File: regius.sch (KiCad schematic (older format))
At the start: 39 parts, among them J1 Conn_01x02, J10 Conn_01x02, J16 Conn_01x04, J7 Conn_01x02, J9 Conn_01x02, SW1 Reset, U5 LM1117-3.3

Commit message: update schematic
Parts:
- removed C? (x8): C_Small, symbol Device:C_Small
- removed D? (x5): D_TVS, symbol Device:D_TVS
- removed J10, J9: Conn_01x02, Connector_PinHeader_2.54mm:PinHeader_1x02_P2.54mm_Vertical, symbol Connector_Generic:Conn_01x02
- removed J16: Conn_01x04, Connector_PinHeader_2.54mm:PinHeader_1x04_P2.54mm_Vertical, symbol Connector_Generic:Conn_01x04
- removed R?: R_Small, symbol Device:R_Small
- added C? (x12): C_Small, symbol Device:C_Small
- added FB?: Ferrite_Bead_Small, symbol Device:Ferrite_Bead_Small
- added R?: R330, Resistor_SMD:R_0603_1608Metric, symbol Device:R
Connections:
- wire segments 150 -> 115
- no-connect marks 0 -> 5
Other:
- moved on the sheet: C10, C8, C9, C?, J1, J7, J?, R1, R2, R3, R6, SW1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

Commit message: debug port
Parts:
- added J?: Conn_02x05_Counter_Clockwise, symbol Connector_Generic:Conn_02x05_Counter_Clockwise
- added R?: R1K, Resistor_SMD:R_0603_1608Metric, symbol Device:R
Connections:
- wire segments 115 -> 132
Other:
- moved on the sheet: R1, R2, R3
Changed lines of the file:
@@
 Text Label 22400 6600 0    50   ~ 0
 txd0
-Text Label 12400 6000 0    50   ~ 0
+Text Label 12850 6550 3    50   ~ 0
 RESET
 Wire Wire Line
@@
 	21500 6700 22400 6700
 Wire Wire Line
-	9850 10100 9850 11000
-Wire Wire Line
-	9950 10100 9950 10900
+	8100 11100 8100 12000
+Wire Wire Line
+	8200 11100 8200 11900
 $Comp
 L Mechanical:MountingHole H4
@@
 	1    0    0    -1
 $EndComp
-Text Label 9850 11000 3    50   ~ 0
+Text Label 8100 12000 3    50   ~ 0
 sda
 $Comp
@@
 L Device:LED_ARGB D1
 U 1 1 5C5B0455
-P 9650 7950
-F 0 "D1" H 9650 7483 50  0000 C CNN
-F 1 "LED_ARGB" H 9650 7574 50  0000 C CNN
-F 2 "LED_SMD:LED_RGB_1210" H 9650 7900 50  0001 C CNN
-F 3 "~" H 9650 7900 50  0001 C CNN
-	1    9650 7950
+P 5450 10700
+F 0 "D1" H 5450 10233 50  0000 C CNN
+F 1 "LED_ARGB" H 5450 10324 50  0000 C CNN
+F 2 "LED_SMD:LED_RGB_1210" H 5450 10650 50  0001 C CNN
+F 3 "~" H 5450 10650 50  0001 C CNN
+	1    5450 10700
 	-1   0    0    1
 $EndComp
@@
 L Device:R R1
 U 1 1 5C5B0BC3
-P 10250 7750
-F 0 "R1" V 10150 7650 50  0000 C CNN
-F 1 "75" V 10150 7850 50  0000 C CNN
-F 2 "Resistor_SMD:R_0603_1608Metric" V 10180 7750 50  0001 C CNN
-F 3 "~" H 10250 7750 50  0001 C CNN
-	1    10250 7750
+P 6050 10500
+F 0 "R1" V 5950 10400 50  0000 C CNN
+F 1 "75" V 5950 10600 50  0000 C CNN
+F 2 "Resistor_SMD:R_0603_1608Metric" V 5980 10500 50  0001 C CNN
+F 3 "~" H 6050 10500 50  0001 C CNN
+	1    6050 10500
 	0    1    1    0
 $EndComp
@@
 L Device:R R2
 U 1 1 5C5B0E5A
-P 10250 7950
-F 0 "R2" V 10150 7850 50  0000 C CNN
-F 1 "75" V 10150 8050 50  0000 C CNN
-F 2 "Resistor_SMD:R_0603_1608Metric" V 10180 7950 50  0001 C CNN
-F 3 "~" H 10250 7950 50  0001 C CNN
-	1    10250 7950
+P 6050 10700
+F 0 "R2" V 5950 10600 50  0000 C CNN
+F 1 "75" V 5950 10800 50  0000 C CNN
+F 2 "Resistor_SMD:R_0603_1608Metric" V 5980 10700 50  0001 C CNN
+F 3 "~" H 6050 10700 50  0001 C CNN
+	1    6050 10700
 	0    1    1    0
 $EndComp
@@
 L Device:R R3
 U 1 1 5C5B10FB
-P 10250 8150
-F 0 "R3" V 10150 8050 50  0000 C CNN
-F 1 "100" V 10150 8250 50  0000 C CNN
-F 2 "Resistor_SMD:R_0603_1608Metric" V 10180 8150 50  0001 C CNN
-F 3 "~" H 10250 8150 50  0001 C CNN
-	1    10250 8150
-	0    1    1    0
-$EndComp
-Wire Wire Line
-	11150 7850 10400 7850
-Wire Wire Line
-	10400 7850 10400 7750
-Wire Wire Line
-	11150 7950 10400 7950
-Wire Wire Line
-	11150 8050 10400 8050
-Wire Wire Line
-	10400 8050 10400 8150
-Wire Wire Line
-	10100 7750 9850 7750
-Wire Wire Line
-	10100 7950 9850 7950
-Wire Wire Line
-	10100 8150 9850 8150
-Wire Wire Line
-	9450 7950 9350 7950
-Wire Wire Line
-	9350 7950 9350 9000
-Text Label 9950 10900 3    50   ~ 0
+P 6050 10900
+F 0 "R3" V 5950 10800 50  0000 C CNN
+F 1 "100" V 5950 11000 50  0000 C CNN
+F 2 "Resistor_SMD:R_0603_1608Metric" V 5980 10900 50  0001 C CNN
+F 3 "~" H 6050 10900 50  0001 C CNN
+	1    6050 10900
+	0    1    1    0
+$EndComp
+Wire Wire Line
+	6950 10600 6200 10600
+Wire Wire Line
+	6200 10600 6200 10500
+Wire Wire Line
+	6950 10700 6200 10700
+Wire Wire Line
+	6950 10800 6200 10800
+Wire Wire Line
+	6200 10800 6200 10900
+Wire Wire Line
+	5900 10500 5650 10500
+Wire Wire Line
+	5900 10700 5650 10700
+Wire Wire Line
+	5900 10900 5650 10900
+Wire Wire Line
+	5250 10700 5150 10700
+Wire Wire Line
+	5150 10700 5150 11750
+Text Label 8200 11900 3    50   ~ 0
 scl
 $Comp
@@
 	19400 6100 19150 6100
 Wire Wire Line
-	11850 6000 12400 6000
-Wire Wire Line
 	11850 6300 11850 6500
 Wire Wire Line
@@
 Wire Wire Line
 	19700 5300 19700 5050
+$Comp
+L Connector_Generic:Conn_02x05_Counter_Clockwise J?
+U 1 1 5CA08950
+P 13900 5500
+F 0 "J?" H 13950 5917 50  0000 C CNN
+F 1 "Conn_02x05_Counter_Clockwise" H 13950 5826 50  0000 C CNN
+F 2 "" H 13900 5500 50  0001 C CNN
+F 3 "~" H 13900 5500 50  0001 C CNN
+	1    13900 5500
+	1    0    0    -1
+$EndComp
+Wire Wire Line
+	13700 5300 13450 5300
+Wire Wire Line
+	13700 5400 13450 5400
+Wire Wire Line
+	13450 5400 13450 5500
+Wire Wire Line
+	13450 5500 13700 5500
+Connection ~ 13450 5400
+Wire Wire Line
+	13200 5400 13450 5400
+$Comp
+L power:+3.3V #PWR?
+U 1 1 5CA2FE67
+P 13450 5300
+F 0 "#PWR?" H 13450 5150 50  0001 C CNN
+F 1 "+3.3V" V 13465 5428 50  0000 L CNN
+F 2 "" H 13450 5300 50  0001 C CNN
+F 3 "" H 13450 5300 50  0001 C CNN
+	1    13450 5300
+	0    -1   -1   0
+$EndComp
+$Comp
+L power:GND #PWR?
+U 1 1 5CA3C360
+P 13200 5400
+F 0 "#PWR?" H 13200 5150 50  0001 C CNN
+F 1 "GND" H 13205 5227 50  0000 C CNN
+F 2 "" H 13200 5400 50  0001 C CNN
+F 3 "" H 13200 5400 50  0001 C CNN
+	1    13200 5400
+	0    1    1    0
+$EndComp
+Wire Wire Line
+	14200 6000 14200 5700
+Wire Wire Line
+	11850 6000 12850 6000
+Connection ~ 12850 6000
+Wire Wire Line
+	12850 6000 14200 6000
+Wire Wire Line
+	12850 6000 12850 6550
+Wire Wire Line
+	14900 6600 14900 5500
+Wire Wire Line
+	14900 5500 14200 5500
+Wire Wire Line
+	15100 6600 15100 5400
+Wire Wire Line
+	15100 5400 14700 5400
+Wire Wire Line
+	14200 5300 15000 5300
+Wire Wire Line
+	15000 5300 15000 6600
+Wire Wire Line
+	14700 5400 14700 4950
+Connection ~ 14700 5400
+Wire Wire Line
+	14700 5400 14200 5400
+$Comp
+L Device:R R?
+U 1 1 5CACE498
+P 14700 4800
+F 0 "R?" V 14493 4800 50  0000 C CNN
+F 1 "R1K" V 14584 4800 50  0000 C CNN
+F 2 "Resistor_SMD:R_0603_1608Metric" V 14630 4800 50  0001 C CNN
+F 3 "~" H 14700 4800 50  0001 C CNN
+	1    14700 4800
+	-1   0    0    1
+$EndComp
+Wire Wire Line
+	14700 4650 14700 4400
+$Comp
+L power:+3.3V #PWR?
+U 1 1 5CAD68D3
+P 14700 4400
+F 0 "#PWR?" H 14700 4250 50  0001 C CNN
+F 1 "+3.3V" H 14715 4573 50  0000 C CNN
+F 2 "" H 14700 4400 50  0001 C CNN
+F 3 "" H 14700 4400 50  0001 C CNN
+	1    14700 4400
+	1    0    0    -1
+$EndComp
 $EndSCHEMATC

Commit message: update design
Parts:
- removed D1: LED_ARGB, LED_SMD:LED_RGB_1210, symbol Device:LED_ARGB
- removed R1, R2: 75, Resistor_SMD:R_0603_1608Metric, symbol Device:R
- removed R3: 100, Resistor_SMD:R_0603_1608Metric, symbol Device:R
- added C? (x4): C_Small, symbol Device:C_Small
- added D? (x2): WS2812B, LED_SMD:LED_WS2812B_PLCC4_5.0x5.0mm_P3.2mm, symbol LED:WS2812B
- added D? (x3): LED_Small, symbol Device:LED_Small
- added R? (x3): R1K, Resistor_SMD:R_0603_1608Metric, symbol Device:R
- added Y?: Crystal, symbol Device:Crystal
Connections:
- net labels removed: RESET, rxd0, scl, sda, txd0
- wire segments 132 -> 169
- no-connect marks 5 -> 0
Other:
- moved on the sheet: C10, C9, C?, FB?, R?, U5

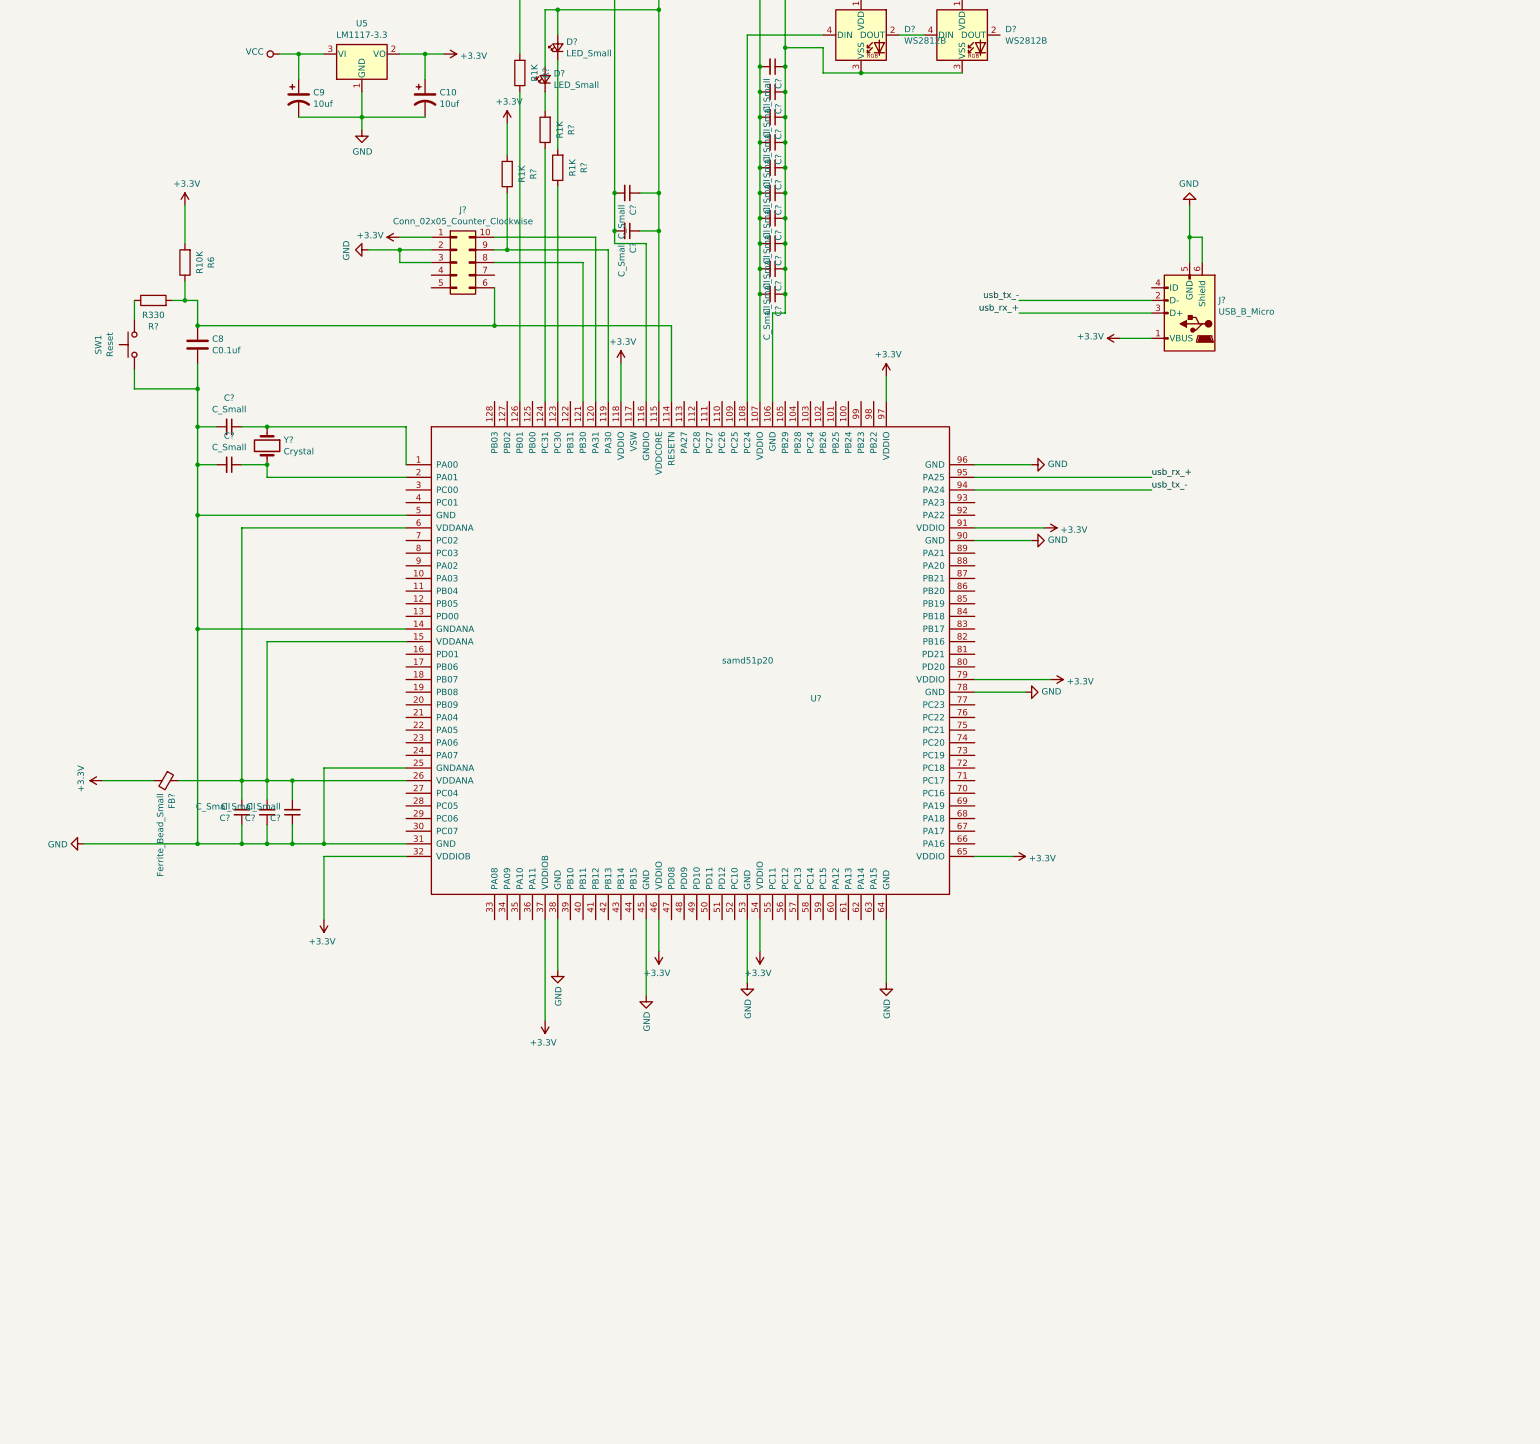
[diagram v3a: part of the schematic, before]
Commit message: update schematic
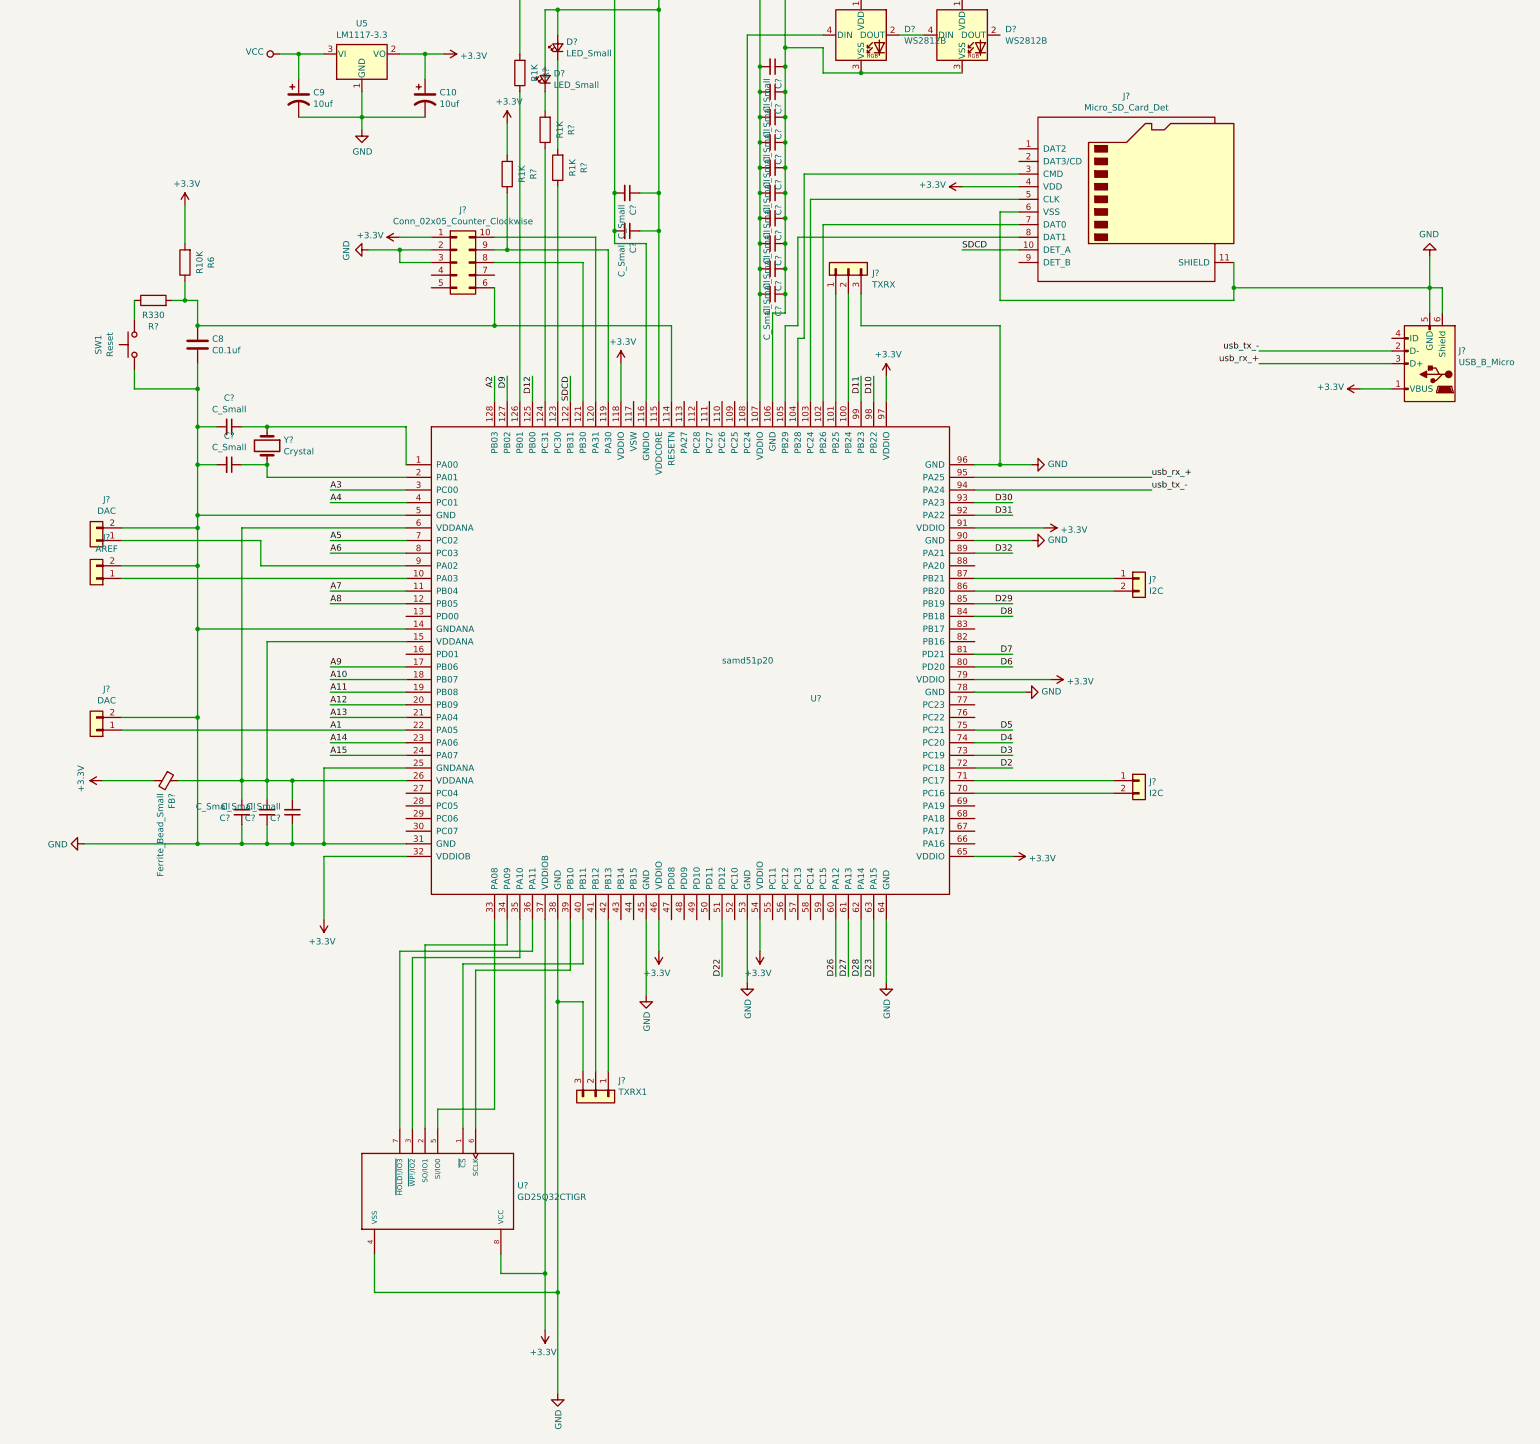
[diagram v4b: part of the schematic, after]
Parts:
- added J?: AREF, symbol Connector_Generic:Conn_01x02
- added J?: TXRX, symbol Connector_Generic:Conn_01x03
- added J?: TXRX1, symbol Connector_Generic:Conn_01x03
- added J? (x2): DAC, symbol Connector_Generic:Conn_01x02
- added J? (x2): I2C, symbol Connector_Generic:Conn_01x02
- added J?: Micro_SD_Card_Det, symbol Connector:Micro_SD_Card_Det
- added U?: GD25Q32CTIGR, SOIC127P600X175-8N, symbol GD25Q32CTIGR:GD25Q32CTIGR
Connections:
- net +3V3: now also J?.4 (VDD), U?.8 (VCC)
- net GND: now also J?.11 (SHIELD), J?.2 (Pin_2), J?.2 (Pin_2), J?.2 (Pin_2), J?.3 (Pin_3), J?.3 (Pin_3), J?.6 (VSS), U?.4 (VSS)
- net at U?.10 (PA03): now also J?.1 (Pin_1)
- net at U?.100 (PB24): now also J?.2 (Pin_2)
- net at U?.101 (PB25): now also J?.1 (Pin_1)
- net at U?.102 (PB26): now also J?.7 (DAT0)
- net at U?.103 (PC24): now also J?.5 (CLK)
- net at U?.104 (PB28): now also J?.3 (CMD)
- net at U?.105 (PB29): now also J?.8 (DAT1)
- net A7: now reaches U?.11 (PB04)
- net A8: now reaches U?.12 (PB05)
- net SDCD: now reaches U?.122 (PB31)
- net SDCD: now also J?.10 (DET_A)
- net D12: now reaches U?.125 (PB00)
- net D9: now reaches U?.127 (PB02)
- net A2: now reaches U?.128 (PB03)
- net A9: now reaches U?.17 (PB06)
- net A10: now reaches U?.18 (PB07)
- net A11: now reaches U?.19 (PB08)
- net A12: now reaches U?.20 (PB09)
- net A13: now reaches U?.21 (PA04)
- net A1: now reaches U?.22 (PA05)
- net A1: now also J?.1 (Pin_1)
- net A14: now reaches U?.23 (PA06)
- net A15: now reaches U?.24 (PA07)
- net A3: now reaches U?.3 (PC00)
- net at U?.33 (PA08): now also U?.5 (SI/IO0)
- net at U?.34 (PA09): now also U?.2 (SO/IO1)
- net at U?.35 (PA10): now also U?.3 (~WP!/IO2~)
- net at U?.36 (PA11): now also U?.7 (~HOLD!/IO3~)
- net at U?.39 (PB10): now also U?.6 (SCLK)
- net A4: now reaches U?.4 (PC01)
- net at U?.40 (PB11): now also U?.1 (~CS~)
- net at U?.41 (PB12): now also J?.2 (Pin_2)
- net at U?.42 (PB13): now also J?.1 (Pin_1)
- net D22: now reaches U?.51 (PD12)
- net D26: now reaches U?.60 (PA12)
- net D27: now reaches U?.61 (PA13)
- net D28: now reaches U?.62 (PA14)
- net D23: now reaches U?.63 (PA15)
- net A5: now reaches U?.7 (PC02)
- net at U?.70 (PC16): now also J?.2 (Pin_2)
- net at U?.71 (PC17): now also J?.1 (Pin_1)
- net D2: now reaches U?.72 (PC18)
- net D3: now reaches U?.73 (PC19)
- net D4: now reaches U?.74 (PC20)
- net D5: now reaches U?.75 (PC21)
- net A6: now reaches U?.8 (PC03)
- net D6: now reaches U?.80 (PD20)
- net D7: now reaches U?.81 (PD21)
- net D8: now reaches U?.84 (PB18)
- net D29: now reaches U?.85 (PB19)
- net at U?.86 (PB20): now also J?.2 (Pin_2)
- net at U?.87 (PB21): now also J?.1 (Pin_1)
- net D32: now reaches U?.89 (PA21)
- net at U?.9 (PA02): now also J?.1 (Pin_1)
- net D31: now reaches U?.92 (PA22)
- net D30: now reaches U?.93 (PA23)
- net D10: now reaches U?.98 (PB22)
- net D11: now reaches U?.99 (PB23)
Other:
- moved on the sheet: J?
